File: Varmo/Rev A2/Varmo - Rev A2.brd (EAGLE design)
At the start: 131 x 87 mm, 103 parts, among them J1 22-05-7028-02, J2 22-05-7028-02, J3 22-05-7038-03, J4 22-05-7038-03, J5 22-05-7038-03, J6 22-05-7038-03, J7 22-05-7028-02, J8 22-05-7028-02, J9 22-05-7038-03, T1 MMBT2222AL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

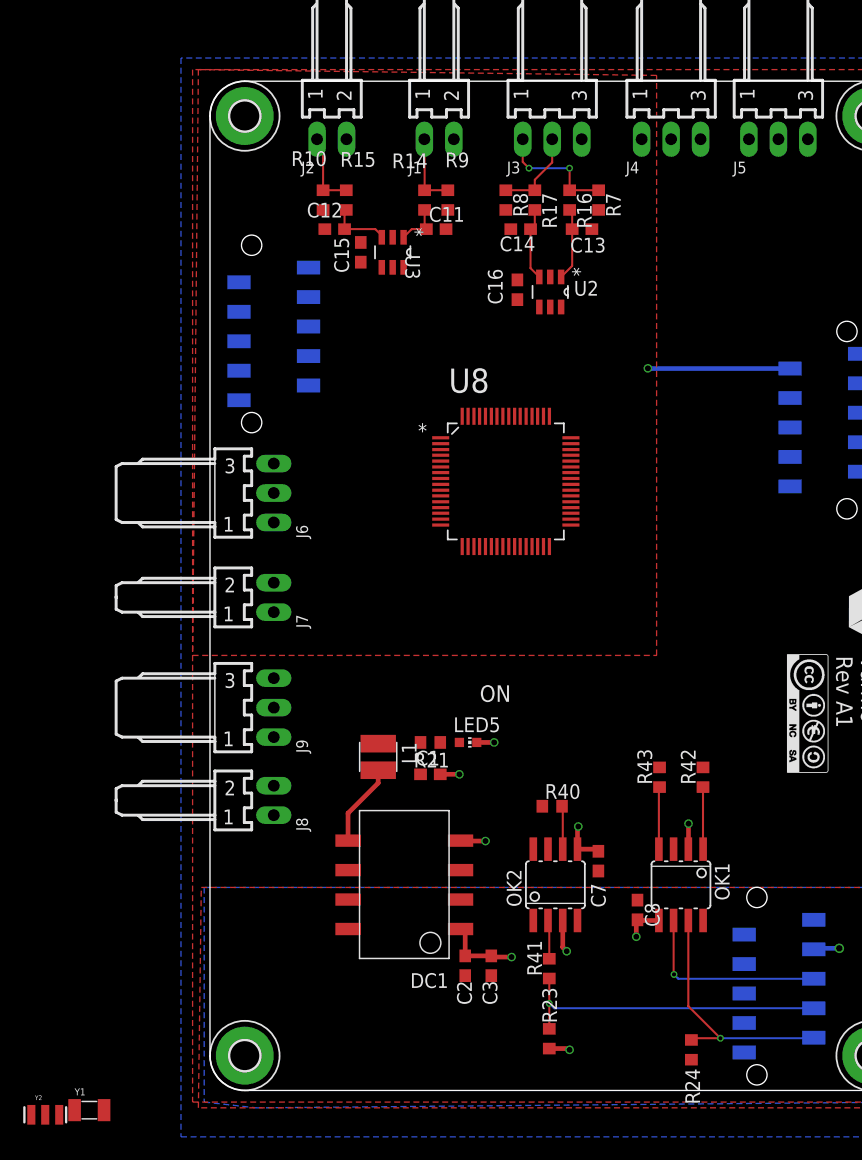
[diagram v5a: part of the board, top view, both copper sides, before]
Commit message: Add the +3V3 LDO and change the position of the connector
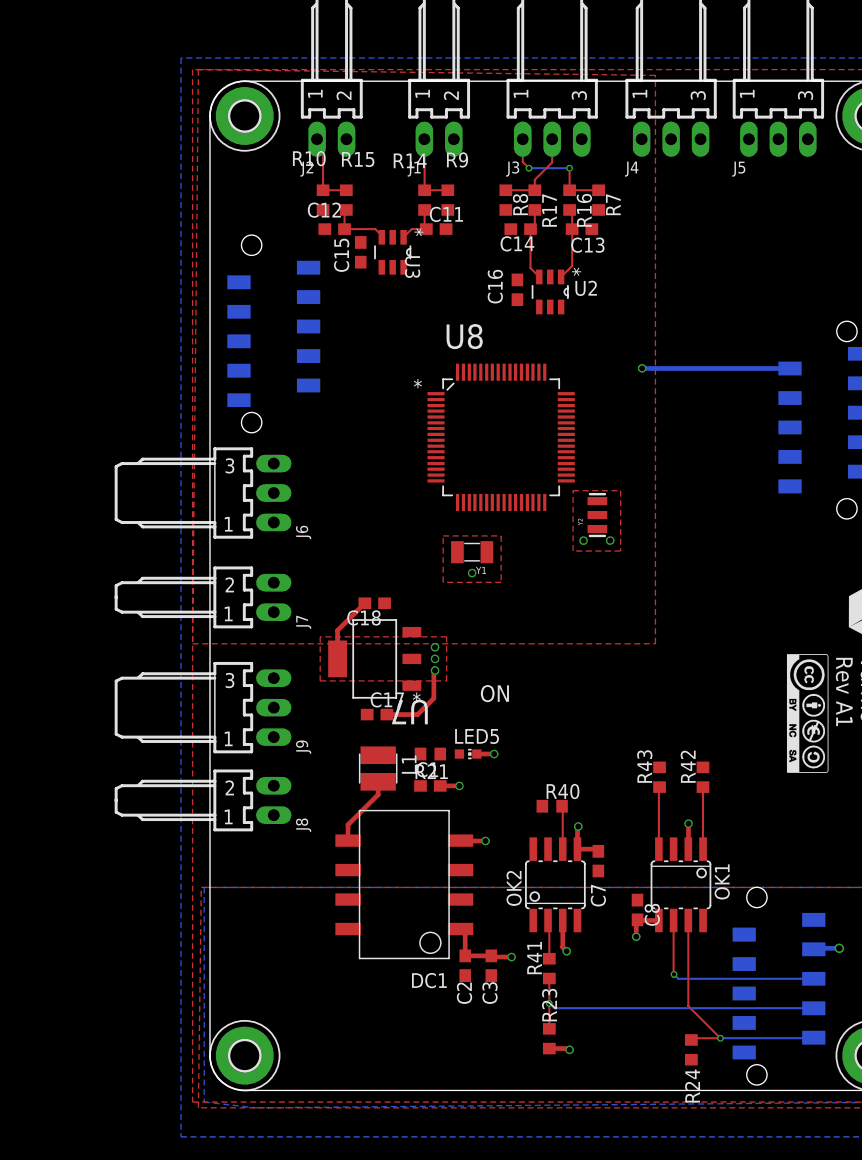
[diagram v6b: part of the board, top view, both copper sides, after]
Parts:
- added C17, C18: 0.1uF, rcl:C0603
- added U7: TC1262-3.3, microchip-6:SOT230P700X180-4N
- moved Y2 70.3 mm to (33.4, 49.6), turned to 90 degrees
- moved Y1 58.3 mm to (22.6, 46.4), turned to 180 degrees
- moved U8 3.82 mm to (25.1, 56.3)
- moved C1 1.00 mm to (19.0, 26.2)
- moved L1 1.00 mm to (14.5, 27.8)
- moved LED5 1.00 mm to (22.2, 29.0)
- moved R21 1.00 mm to (19.0, 29.0)
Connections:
- net +3V3: now also C18.1, U7.3
- net +5V/1: now also C17.1, U7.1
- net GND1: now also C17.2, C18.2, U7.2, U7.4
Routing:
- net GND1: track 32.5 -> 45.4 mm, vias 17 -> 23
- net N$1: track 7.15 -> 6.15 mm

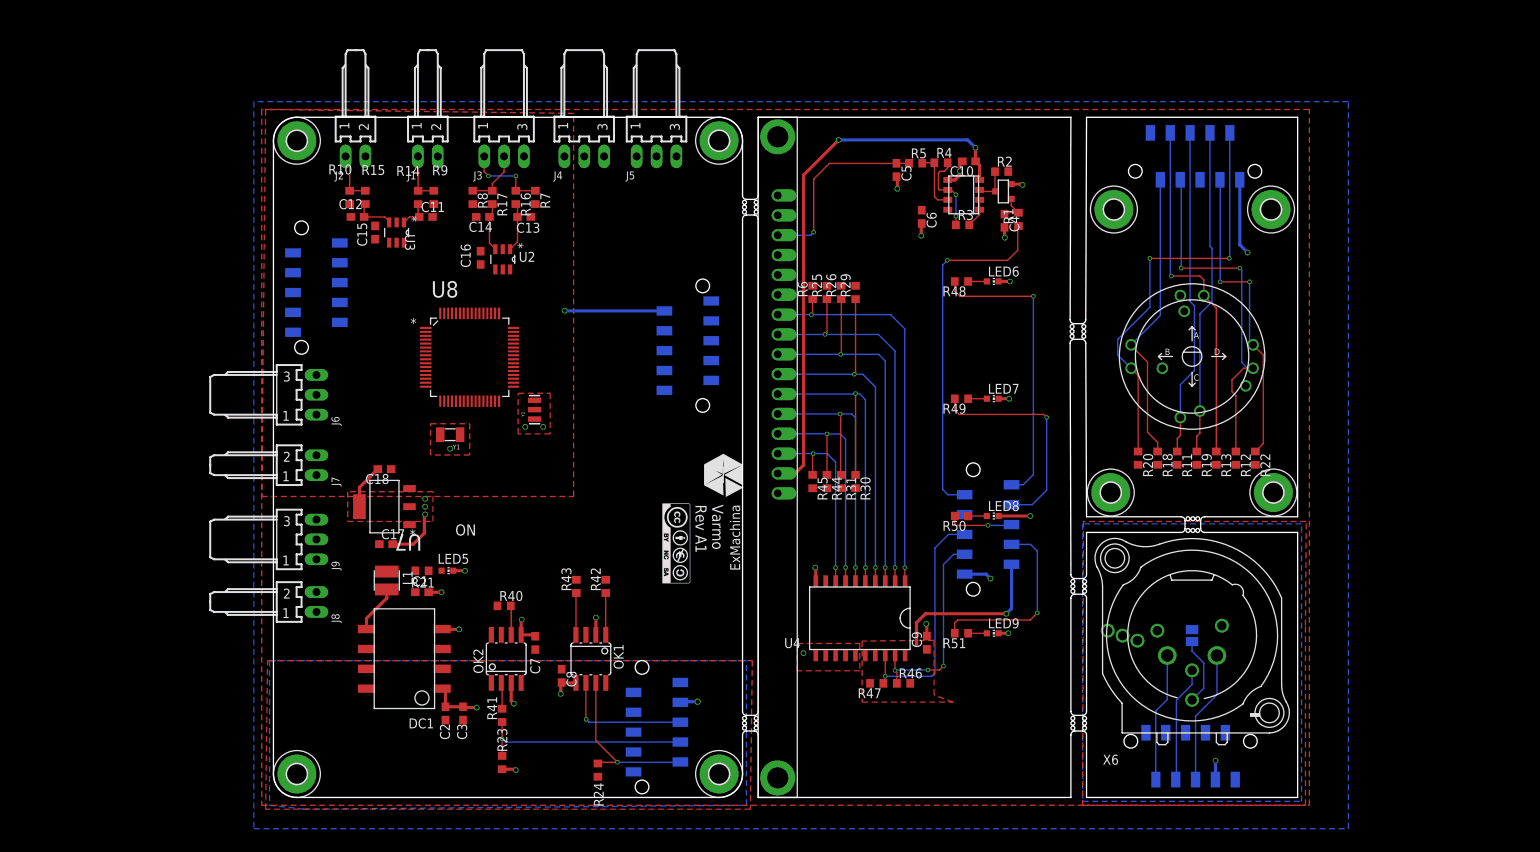
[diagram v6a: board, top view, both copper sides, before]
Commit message: Move the hole of the cpu panel
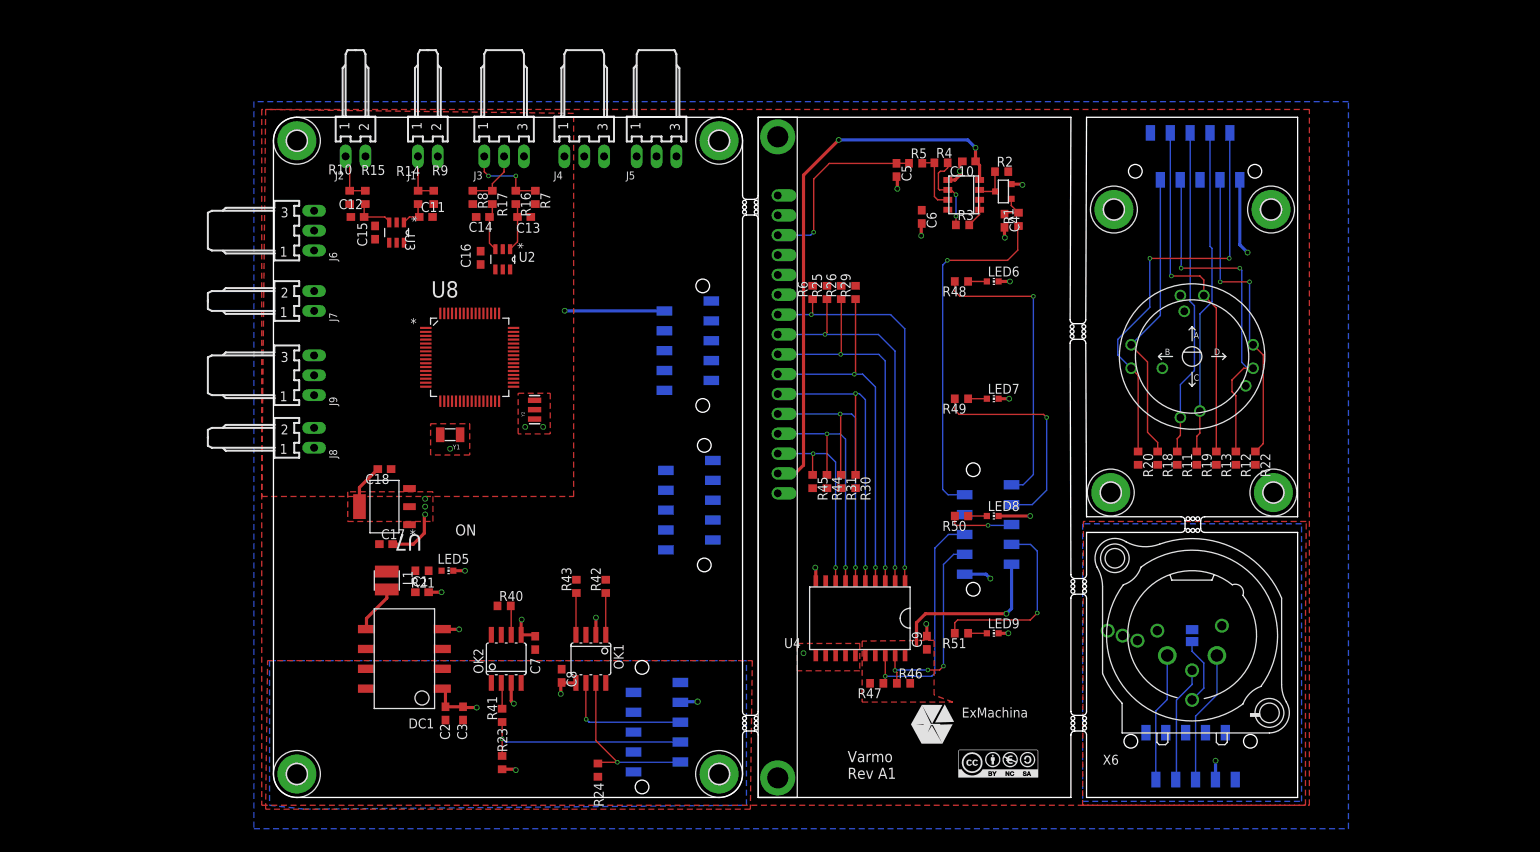
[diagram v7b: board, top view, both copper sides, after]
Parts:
- moved X1 56.1 mm to (56.2, 43.1), turned to 270 degrees
- moved U$1 49.9 mm to (92.7, 4.30), turned to 0 degrees
- moved U$6 41.6 mm to (84.2, 9.34), turned to 0 degrees
- moved J6 21.0 mm to (5.20, 72.5)
- moved J7 21.0 mm to (5.20, 63.5)
- moved J8 21.0 mm to (5.20, 46.0)
- moved J9 21.0 mm to (5.20, 54.0)

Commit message: Place the connector on the varmo, reduce the size of the LCD Panel, Place the hole on the joystick panel
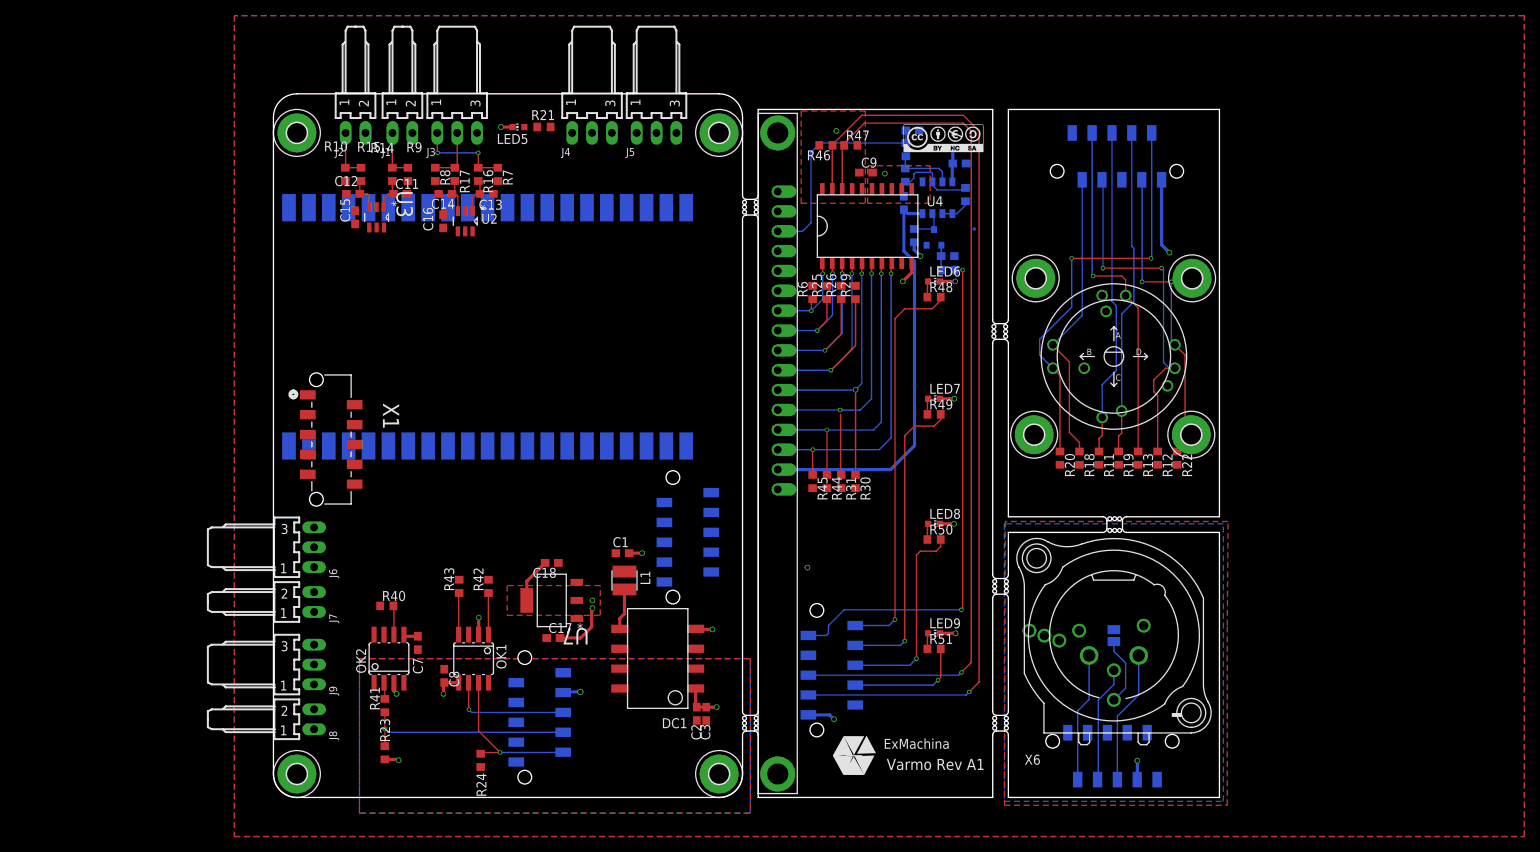
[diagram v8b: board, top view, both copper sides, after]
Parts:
- removed Y1: 32.768kHz, 12.5pF, crystal:ABS07
- removed Y2: 8MHz, resonator:RESONATOR-SMD
- U8: value MK20DX256VLH7 -> M20DX256; device freescale:QFP50P1200X1200X160-64N -> custom:MK_CUSTOM
- moved U$1 80.3 mm to (85.7, 84.3)
- moved R46 69.5 mm to (70.7, 83.4), turned to 180 degrees
- moved R47 68.9 mm to (73.8, 83.4), turned to 0 degrees
- moved C9 60.6 mm to (75.8, 79.9), turned to 0 degrees
- moved R21 58.9 mm to (34.6, 85.8), turned to 0 degrees
- moved LED5 57.5 mm to (31.4, 85.8), turned to 90 degrees
- moved X1 52.5 mm to (4.40, 51.5), flipped to the top
- moved U4 50.2 mm to (75.9, 73.1), turned to 0 degrees
- moved J6 40.5 mm to (5.20, 32.0)
- moved J7 38.5 mm to (5.20, 25.0)
- moved J9 37.0 mm to (5.20, 17.0)
- moved U6 36.4 mm to (50.0, 27.6), turned to 90 degrees
- moved J8 36.0 mm to (5.20, 10.0)
- moved DC1 32.4 mm to (49.1, 17.8)
- moved C2 32.2 mm to (54.1, 10.7)
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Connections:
- removed net N$15: U8.19, Y1.2
- removed net N$16: U8.20, Y1.1
- removed net N$30: U8.33, Y2.3
- removed net N$31: U8.32, Y2.1
- removed net VBAT: U8.21
- removed net VDD: U8.3, U8.48
- removed net VDDA: U8.13
- removed net VDD_2: U8.30
- net +3V3: now also U8.21, U8.22
- net +5V: now also U8.42
- net GND: now also U8.20, U8.23
- net GND1: no longer Y2.2
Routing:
- net SDA: track 26.7 -> 119.8 mm, vias 3 -> 1
- net SCL: track 31.1 -> 113.2 mm
- net D0: track 51.3 -> 12.5 mm
- net +3V3: track 34.2 -> 0.00 mm, vias 2 -> 1
- net D1: track 49.9 -> 19.0 mm
- net D2: track 49.4 -> 25.5 mm
- net PWM_CONTRASTE: track 45.3 -> 66.1 mm, vias 1 -> 2
- net LED_STATUS_3: track 8.42 -> 25.9 mm
- net VEE: track 69.5 -> 52.1 mm, vias 2 -> 0
- net D3: track 47.7 -> 32.0 mm
- net D7: track 25.9 -> 40.7 mm
- net LED_STATUS_1: track 37.7 -> 51.1 mm
- net GND1: track 45.4 -> 33.2 mm, vias 23 -> 13
- net LED_STATUS_2: track 28.2 -> 38.9 mm
- net LED_STATUS_4: track 24.0 -> 15.0 mm
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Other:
- board size 131 x 87 mm -> 121 x 90 mm
- board text removed: "ON"
